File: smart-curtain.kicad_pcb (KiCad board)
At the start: 4 copper layers, 42 x 42 mm, 19 parts, among them IC1 AS5040-ASST, IC2 ESP32-S3-MINI-1-N8, IC3 MPM3612GLQ-33-P, J1 USB4110-GF-A, J2 Limit, J3 Motor, J4 Qwiic 1, J5 Qwiic 2, U1 TMC2209-LA-T, U2 TPS25730DREFR

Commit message: Add AS5600
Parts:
- removed IC2: ESP32-S3-MINI-1-N8, Samacsys:ESP32S3MINI1N8
- removed IC3: MPM3612GLQ-33-P, Samacsys:MPM3612GLQ33P
- added R20: 10k, Resistor_SMD:R_0805_2012Metric, F.Cu at (107.6, 106.2)
- added R21: 3.3k, Resistor_SMD:R_0805_2012Metric, F.Cu at (107.6, 109.1)
- added R22: 3.3k, Resistor_SMD:R_0805_2012Metric, F.Cu at (107.6, 112.0)
- added R25: 4.7k, Resistor_SMD:R_0805_2012Metric, F.Cu at (107.6, 115.0)
- added U3: TPS25730DREFR, Samacsys:TPS25730DREFR, F.Cu at (141.9, 106.6)
- added U4: AS5600L, Samacsys:SOIC127P600X175-8N, B.Cu at (143.5, 96.5)
- IC1: value AS5040-ASST -> ESP32-S3-MINI-1-N8; footprint Samacsys:SOP65P778X199-16N -> Samacsys:ESP32S3MINI1N8; moved to F.Cu
- R1: value R -> 0
- R2: value 4.7k -> 0
- R3: value 3.3k -> 0
- R4: value 3.3k -> 20k
- U2: value TPS25730DREFR -> MPM3612GLQ-33-P; footprint Samacsys:TPS25730DREFR -> Samacsys:MPM3612GLQ33P
- moved R1 41.6 mm to (111.5, 106.2)
- moved R2 22.9 mm to (107.6, 103.0)
- moved U2 9.67 mm to (150.0, 112.0)
- moved IC1 8.56 mm to (135.5, 93.5)
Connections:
- IC1 pad 1: unconnected-(IC1-MAGINCN-Pad1) -> GND
- IC1 pad 10: unconnected-(IC1-CLK-Pad10) -> /PLUG_FLIP
- IC1 pad 11: unconnected-(IC1-CSN-Pad11) -> /FAULT_IN
- IC1 pad 12: unconnected-(IC1-PWM_LSB-Pad12) -> /SDA
- IC1 pad 13: unconnected-(IC1-NC_2-Pad13) -> /SCL
- IC1 pad 14: unconnected-(IC1-NC_3-Pad14) -> /STEP
- IC1 pad 15: unconnected-(IC1-VDD3V3-Pad15) -> /DIR
- IC1 pad 16: unconnected-(IC1-VDD5V-Pad16) -> /MS1
- IC1 pad 2: unconnected-(IC1-MAGDECN-Pad2) -> GND
- IC1 pad 3: unconnected-(IC1-A_LSB_U-Pad3) -> +3V3
- IC1 pad 4: unconnected-(IC1-B_DIR_V-Pad4) -> Net-(IC1-IO0)
- IC1 pad 6: unconnected-(IC1-INDEX_W-Pad6) -> /AS5600_DIR
- IC1 pad 7: unconnected-(IC1-VSS-Pad7) -> /NTC
- IC1 pad 8: unconnected-(IC1-PROG-Pad8) -> /DBG_ACC
- IC1 pad 9: unconnected-(IC1-DO-Pad9) -> /CAP_MIS
- J1 pad A4: Net-(U2-VBUS_1) -> Net-(U3-VBUS_1)
- J1 pad A9: Net-(U2-VBUS_1) -> Net-(U3-VBUS_1)
- J1 pad B4: Net-(U2-VBUS_1) -> Net-(U3-VBUS_1)
- J1 pad B9: Net-(U2-VBUS_1) -> Net-(U3-VBUS_1)
- R1 pad 1: Net-(IC2-IO46) -> /LDO_1V5
- R1 pad 2: GND -> /ADCIN1
- R2 pad 1: Net-(IC2-EN) -> /LDO_3V3
- R2 pad 2: +3V3 -> /ADCIN1
- R3 pad 1: +3V3 -> /ADCIN1
- R3 pad 2: /SDA -> GND
- R4 pad 1: +3V3 -> +5V
- R4 pad 2: /SCL -> Net-(R4-Pad2)
- R5 pad 2: /FAULT_IN -> /MOTOR_~{EN}
- U2 pad 1: /LDO_3V3 -> Net-(U2-EN)
- U2 pad 2: /ADCIN1 -> /PPHV
- U2 pad 3: /ADCIN2 -> GND
- U2 pad 4: /LDO_1V5 -> +3V3
- U2 pad 5: /ADCIN3 -> +3V3
- U2 pad 6: /CAP_MIS -> Net-(U2-VOUT_S)
- U2 pad 7: /ADCIN4 -> unconnected-(U2-PG-Pad7)
- U2 pad 8: /SDA -> unconnected-(U2-VCC-Pad8)
- U2 pad 9: /SCL -> GND

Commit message: Update smart-curtain.kicad_pcb
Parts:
- added C1: 22uF, Capacitor_SMD:C_0402_1005Metric, F.Cu at (102.6, 75.7)
- added C10: 330pF, Capacitor_SMD:C_0402_1005Metric, F.Cu at (105.5, 79.6)
- added C11: 0.01uF, Capacitor_SMD:C_0402_1005Metric, F.Cu at (105.5, 81.6)
- added C12: 0.01uF, Capacitor_SMD:C_0402_1005Metric, F.Cu at (105.5, 83.5)
- added C13: 10uF, Capacitor_SMD:C_0402_1005Metric, F.Cu at (105.5, 85.5)
- added C14: 0.1uF 35V, Capacitor_SMD:C_0402_1005Metric, F.Cu at (105.5, 87.5)
- added C15: 0.1uF 35V, Capacitor_SMD:C_0402_1005Metric, F.Cu at (108.3, 75.7)
- added C16: 0.1uF 35V, Capacitor_SMD:C_0402_1005Metric, F.Cu at (108.3, 77.6)
- added C17: 0.1uF 35V, Capacitor_SMD:C_0402_1005Metric, F.Cu at (108.3, 79.6)
- added C18: 0.1uF 35V, Capacitor_SMD:C_0402_1005Metric, F.Cu at (108.3, 81.6)
- added C19: 100uF 35V, Capacitor_SMD:CP_Elec_4x3, F.Cu at (96.3, 91.5)
- added C2: 22uF, Capacitor_SMD:C_0402_1005Metric, F.Cu at (102.6, 77.6)
- added C20: 10uF, Capacitor_SMD:C_0402_1005Metric, F.Cu at (108.3, 83.5)
- added C21: 22uF, Capacitor_SMD:C_0402_1005Metric, F.Cu at (108.3, 85.5)
- added C22: 10uF, Capacitor_SMD:C_0402_1005Metric, F.Cu at (108.3, 87.5)
- added C23: 22uF, Capacitor_SMD:C_0402_1005Metric, F.Cu at (111.2, 75.7)
- added C24: 10uF, Capacitor_SMD:C_0402_1005Metric, F.Cu at (111.2, 77.6)
- added C25: 100nF, Capacitor_SMD:C_0402_1005Metric, F.Cu at (111.2, 79.6)
- added C26: 0.1 uF, Capacitor_SMD:C_0402_1005Metric, F.Cu at (111.2, 81.6)
- added C27: 0.1 uF, Capacitor_SMD:C_0402_1005Metric, F.Cu at (111.2, 83.5)
- added C28: 0.1 uF, Capacitor_SMD:C_0402_1005Metric, F.Cu at (111.2, 85.5)
- added C3: 22nF 50V, Capacitor_SMD:C_0402_1005Metric, F.Cu at (102.6, 79.6)
- added C4: 4.7uF, Capacitor_SMD:C_0402_1005Metric, F.Cu at (102.6, 81.6)
- added C5: 0.1uF, Capacitor_SMD:C_0402_1005Metric, F.Cu at (102.6, 83.5)
- added C6: 0.1uF, Capacitor_SMD:C_0402_1005Metric, F.Cu at (102.6, 85.5)
- added C7: 0.01uF, Capacitor_SMD:C_0402_1005Metric, F.Cu at (102.6, 87.5)
- added C8: 0.01uF, Capacitor_SMD:C_0402_1005Metric, F.Cu at (105.5, 75.7)
- added C9: 330pF, Capacitor_SMD:C_0402_1005Metric, F.Cu at (105.5, 77.6)
- added D1: LED Green, Diode_SMD:D_0402_1005Metric, F.Cu at (109.5, 95.5)
- added R10: 0, Resistor_SMD:R_0402_1005Metric, F.Cu at (93.9, 83.6)
- added R11: 0, Resistor_SMD:R_0402_1005Metric, F.Cu at (93.9, 85.6)
- added R12: 0, Resistor_SMD:R_0402_1005Metric, F.Cu at (93.9, 87.6)
- added R13: 100m, Resistor_SMD:R_0402_1005Metric, F.Cu at (96.8, 75.7)
- added R14: 100m, Resistor_SMD:R_0402_1005Metric, F.Cu at (96.8, 77.7)
- added R15: 10, Resistor_SMD:R_0402_1005Metric, F.Cu at (96.8, 79.6)
- added R16: 0, Resistor_SMD:R_0402_1005Metric, F.Cu at (96.8, 81.6)
- added R17: 0, Resistor_SMD:R_0402_1005Metric, F.Cu at (96.8, 83.6)
- added R18: 0, Resistor_SMD:R_0402_1005Metric, F.Cu at (96.8, 85.6)
- added R19: 10k, Resistor_SMD:R_0402_1005Metric, F.Cu at (96.8, 87.6)
- added R23: 10k, Resistor_SMD:R_0402_1005Metric, F.Cu at (99.7, 75.7)
- added R24: 1k, Resistor_SMD:R_0402_1005Metric, F.Cu at (99.7, 77.7)
- added R26: 110, Resistor_SMD:R_0402_1005Metric, F.Cu at (99.7, 79.6)
- added R6: R, Resistor_SMD:R_0402_1005Metric, F.Cu at (93.9, 75.7)
- added R7: 0, Resistor_SMD:R_0402_1005Metric, F.Cu at (93.9, 77.7)
- added R8: 0, Resistor_SMD:R_0402_1005Metric, F.Cu at (93.9, 79.6)
- added R9: 100k, Resistor_SMD:R_0402_1005Metric, F.Cu at (93.9, 81.6)
- added RV1: R_Potentiometer, Potentiometer_SMD:Potentiometer_Bourns_3214W_Vertical, F.Cu at (111.0, 91.5)
- added SW1: Boot, Button_Switch_SMD:SW_Push_1P1T_NO_CK_KMR2, F.Cu at (104.5, 90.8)
- added SW2: Reset, Button_Switch_SMD:SW_Push_1P1T_NO_CK_KMR2, F.Cu at (104.5, 95.4)
- added TH1: 10k NTC, Resistor_SMD:R_0402_1005Metric, F.Cu at (99.7, 81.6)
- R1, R2, R20, R21, R22, R25, R3, R4, R5: footprint Resistor_SMD:R_0805_2012Metric -> Resistor_SMD:R_0402_1005Metric
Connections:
- IC1 pad 5: unconnected-(IC1-IO1-Pad5) -> /STATUS_LED

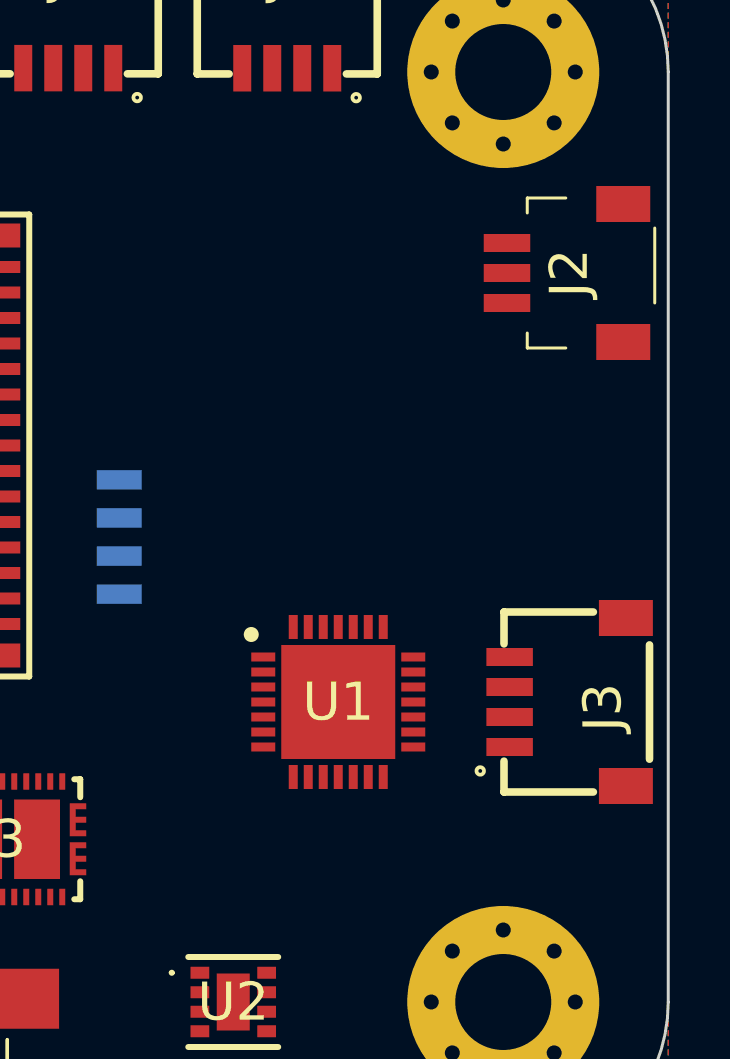
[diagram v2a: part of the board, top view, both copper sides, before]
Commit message: swap J2 with J3
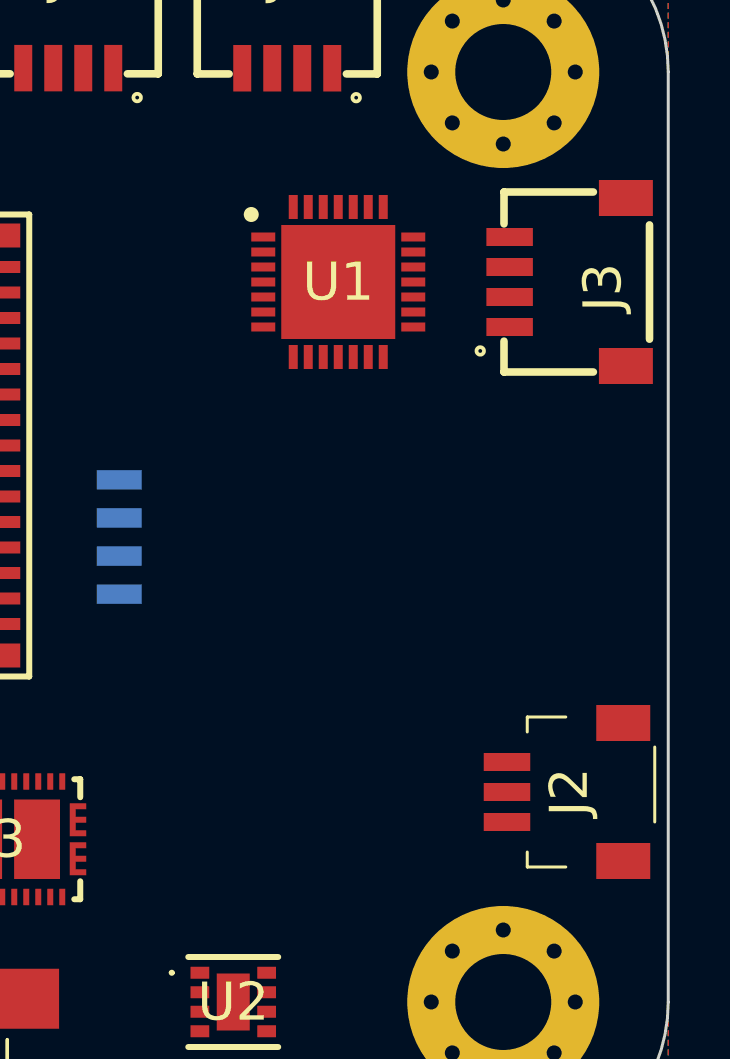
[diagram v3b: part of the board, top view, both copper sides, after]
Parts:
- moved J2 17.3 mm to (161.6, 105.0)
- moved J3 14.0 mm to (163.9, 91.0)
- moved U1 14.0 mm to (153.5, 88.0)
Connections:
- J3 pad 2: /B1 -> /A2
- J3 pad 3: /A2 -> /B1
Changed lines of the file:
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@@
 	(footprint "Samacsys:SM03BSRSSTBLFSN"
 		(layer "F.Cu")
-		(at 161.587 87.7 90)
+		(at 161.587 105 90)
 		(descr "SM03B-SRSS-TB(LF)(SN)-3")
 		(tags "Connector")
@@
 	(footprint "Samacsys:SM04B-SRSS-TB_LFSN_"
 		(layer "F.Cu")
-		(at 163.875 105 90)
+		(at 163.875 91 90)
 		(descr "SM04B-SRSS-TB(LFSN)")
 		(tags "Connector")
@@
 			(size 0.6 1.55)
 			(layers "F.Cu" "F.Mask" "F.Paste")
-			(net 6 "/B1")
+			(net 11 "/A2")
 			(pinfunction "2")
 			(pintype "passive")
@@
 			(size 0.6 1.55)
 			(layers "F.Cu" "F.Mask" "F.Paste")
-			(net 11 "/A2")
+			(net 6 "/B1")
 			(pinfunction "3")
 			(pintype "passive")
@@
 	(footprint "Samacsys:QFN50P500X500X90-29N-D"
 		(layer "F.Cu")
-		(at 153.5 102)
+		(at 153.5 88)
 		(descr "28-LFCSP-5X5X0.9")
 		(tags "Integrated Circuit")
